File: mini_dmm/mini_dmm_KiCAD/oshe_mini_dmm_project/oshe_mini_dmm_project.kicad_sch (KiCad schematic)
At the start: 0 parts

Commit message: added to mini dmm schematic
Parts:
- added R1, R2, R3, R4: R_US, symbol Device:R_US
- added R5: 1, symbol Device:R_US
- added U1: LM358, symbol Amplifier_Operational:LM358
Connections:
- new net: R1.2, R2.1, U1.3 (+)
- new net: R3.1, R5.2
- new net: U1.1, U1.2 (-)
- new net: R3.2, R4.1, U1.5 (+)
- new net: U1.6 (-), U1.7
- new net GND: R2.2, R4.2

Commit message: Added to schematic
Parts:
- added BT1: Battery, symbol Device:Battery
- added F1: 500mA, symbol Device:Fuse_Small
- added F2: 1A, symbol Device:Fuse_Small
- added SW1: SW_DPDT_x2, symbol Switch:SW_DPDT_x2
- added U2: STM32F303CBTx, Package_QFP:LQFP-48_7x7mm_P0.5mm, symbol MCU_ST_STM32F3:STM32F303CBTx
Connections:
- net GND: now also BT1.2 (-)
- net at R1.1: now also F1.2
- net at R5.1: now also F2.2
- net Node_1: now reaches U1.1, U1.2 (-)
- net Node_2: now reaches U1.6 (-), U1.7
- net -3.3V: now reaches U1.4 (V-)
- net +3.3V: now reaches U1.8 (V+)
- net +3.3V: now also SW1.1 (A)
- new net: BT1.1 (+), SW1.2 (B)
- new net: U2.23 (VSS), U2.35 (VSS), U2.47 (VSS)
- no-connect marks 0 -> 1
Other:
- moved on the sheet: R1, R2, R3, R4, R5, U1A, U1B, U1C

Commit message: Made some more updates!
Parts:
- removed U1: LM358, symbol Amplifier_Operational:LM358
- added D1, D2, D3, D4: LED, symbol Device:LED
- added R6, R7, R8, R9: R_US, symbol Device:R_US
- added U1: LM324, Package_SO:SOIC-14_3.9x8.7mm_P1.27mm, symbol Amplifier_Operational:LM324
- renumbered R5 to R1, R1 to R2, R2 to R3, R3 to R4, R4 to R5
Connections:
- net +3.3V: now also U1.4 (V+)
- net -3.3V: now also U1.11 (V-)
- net GND: now also R7.2, R9.2
- net Node_1: now also U1.1, U1.2 (-)
- net Node_2: now also U1.6 (-), U1.7
- net at R2.2, R3.1: now also U1.3 (+)
- net at F2.2, R1.1: now also R6.1
- net at R1.2: now also R8.1; no longer R4.1
- net at R4.2, R5.1: now also U1.5 (+)
- new net: R8.2, R9.1, U1.12 (+)
- new net: R6.2, R7.1, U1.10 (+)
- new net Node_3: U1.8, U1.9 (-)
- new net Node_4: U1.13 (-), U1.14
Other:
- moved on the sheet: BT1, F2, R1, SW1A, U2

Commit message: made some updates
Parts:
- added R10, R11, R12, R13: 1k, symbol Device:R_US
- added SW2: MODE SELECT, symbol Switch:SW_Push
- D1: value LED -> VOLTAGE
- D2: value LED -> CURRENT
- D3: value LED -> RESISTANCE
- D4: value LED -> NEGATIVE
- R2, R4: value R_US -> 9.1MEG
- R3, R5, R7, R9: value R_US -> 1MEG
- R6, R8: value R_US -> 9MEG
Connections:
- net GND: now also R10.1, R11.1, R12.1, R13.1, SW2.2
- net at D4.1 (K): now also R13.2
- net at D4.2 (A): now also U2.13 (PA3)
- net at D2.1 (K): now also R11.2
- net at D2.2 (A): now also U2.11 (PA1)
- net at D3.1 (K): now also R12.2
- net at D3.2 (A): now also U2.12 (PA2)
- net at U2.10 (PA0): now also D1.2 (A)
- net at U2.14 (PA4): now also SW2.1
- net at D1.1 (K): now also R10.2
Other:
- moved on the sheet: BT1, D1, D2, D3, D4, SW1A, U2

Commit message: Updated schematic
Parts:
- added C1, C3, C4: 0.1uF, Capacitor_SMD:C_1206_3216Metric_Pad1.33x1.80mm_HandSolder, symbol Device:C
- added C5, C6: 22pF, Capacitor_SMD:C_1206_3216Metric_Pad1.33x1.80mm_HandSolder, symbol Device:C
- added D5: Green, LED_SMD:LED_1206_3216Metric_Pad1.42x1.75mm_HandSolder, symbol Device:LED
- added J1: FTDI Basic, Connector_PinSocket_2.54mm:PinSocket_1x06_P2.54mm_Vertical, symbol Connector_Generic:Conn_01x06
- added R14: 390, Resistor_SMD:R_1206_3216Metric_Pad1.30x1.75mm_HandSolder, symbol Device:R_US
- added R15: 10k, Resistor_SMD:R_1206_3216Metric_Pad1.30x1.75mm_HandSolder, symbol Device:R_US
- added SW3: PTS526 SK15 SMTR2 LFS, DMM_Footprint_Library:SMT_FS, symbol DMM_Symbol_Library:PTS526_SK15_SMTR2_LFS
- added U3: ATmega328P-A, Package_QFP:TQFP-32_7x7mm_P0.8mm, symbol MCU_Microchip_ATmega:ATmega328P-A
- added Y1: 16MHz, Crystal:Crystal_HC49-U_Vertical, symbol Device:Crystal
- R6, R8: value 9MEG -> 9.1MEG
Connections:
- net GND: now also C1.1, C3.2, C5.2, C6.1, D5.1 (K), J1.5 (Pin_5), J1.6 (Pin_6), SW3.3, SW3.4, U3.21 (GND), U3.3 (GND), U3.5 (GND)
- new net: C6.2, U3.8 (XTAL2/PB7), Y1.1
- new net: C4.1, R15.1, SW3.1, SW3.2, U3.29 (~{RESET}/PC6)
- new net: D5.2 (A), R14.1
- new net: C5.1, U3.7 (XTAL1/PB6), Y1.2
- new net: C1.2, U3.20 (AREF)
- new net +5V: C3.1, J1.4 (Pin_4), R15.2, U3.18 (AVCC), U3.4 (VCC), U3.6 (VCC)
- new net A0: U3.23 (PC0)
- new net A1: U3.24 (PC1)
- new net A2: U3.25 (PC2)
- new net A3: U3.26 (PC3)
- new net A6: U3.19 (ADC6)
- new net A7: U3.22 (ADC7)
- new net D10: U3.14 (PB2)
- new net D2: U3.32 (PD2)
- new net D3: U3.1 (PD3)
- new net D4: U3.2 (PD4)
- new net D5: U3.9 (PD5)
- new net D6: U3.10 (PD6)
- new net D7: U3.11 (PD7)
- new net D8: U3.12 (PB0)
- new net D9: U3.13 (PB1)
- new net DTR: C4.2, J1.1 (Pin_1)
- new net MISO/D12: U3.16 (PB4)
- new net MOSI/D11: U3.15 (PB3)
- new net RXD: J1.3 (Pin_3), U3.30 (PD0)
- new net SCK/D13: R14.2, U3.17 (PB5)
- new net SCL: U3.28 (PC5)
- new net SDA: U3.27 (PC4)
- new net TXD: J1.2 (Pin_2), U3.31 (PD1)
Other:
- note added: "ADD: - Convert arduino from 5V to 3.3V - Charge pump symbol and footprint - Display driver symbol (footprint already created) - resistance measurement stuff?"

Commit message: Made some more changes
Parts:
- removed SW3: PTS526 SK15 SMTR2 LFS, DMM_Footprint_Library:SMT_FS, symbol DMM_Symbol_Library:PTS526_SK15_SMTR2_LFS
- removed U2: STM32F303CBTx, Package_QFP:LQFP-48_7x7mm_P0.5mm, symbol MCU_ST_STM32F3:STM32F303CBTx
- added C2, C4, C5: 1uF, Capacitor_SMD:C_0805_2012Metric_Pad1.18x1.45mm_HandSolder, symbol Device:C
- added J2: DISPLAY, symbol Connector_Generic:Conn_01x12
- added R16: 300, Resistor_SMD:R_0805_2012Metric_Pad1.20x1.40mm_HandSolder, symbol Device:R_US
- added R17: 1k, Resistor_SMD:R_0805_2012Metric_Pad1.20x1.40mm_HandSolder, symbol Device:R_US
- added SW2: PTS526 SK15 SMTR2 LFS, DMM_Footprint_Library:SMT_FS, symbol Mini_DMM_Library:PTS526_SK15_SMTR2_LFS
- added U2: BU91796FS-ME2, Mini_DMM_Footprint_Library:SSOP-A32, symbol Mini_DMM_Library:BU91796FS-ME2
- added U4: LM2664M6, Mini_DMM_Footprint_Library:SOT95P280X145-6N, symbol Mini_DMM_Library:LM2664M6
- BT1: footprint (none) -> Battery:BatteryHolder_Keystone_3034_1x20mm
- C1, C3: footprint Capacitor_SMD:C_1206_3216Metric_Pad1.33x1.80mm_HandSolder -> Capacitor_SMD:C_0805_2012Metric_Pad1.18x1.45mm_HandSolder
- C6: renamed from C4; footprint Capacitor_SMD:C_1206_3216Metric_Pad1.33x1.80mm_HandSolder -> Capacitor_SMD:C_0805_2012Metric_Pad1.18x1.45mm_HandSolder
- C7: renamed from C5; footprint Capacitor_SMD:C_1206_3216Metric_Pad1.33x1.80mm_HandSolder -> Capacitor_SMD:C_0805_2012Metric_Pad1.18x1.45mm_HandSolder
- C8: renamed from C6; footprint Capacitor_SMD:C_1206_3216Metric_Pad1.33x1.80mm_HandSolder -> Capacitor_SMD:C_0805_2012Metric_Pad1.18x1.45mm_HandSolder
- D1, D2, D3, D4: footprint (none) -> LED_SMD:LED_0805_2012Metric_Pad1.15x1.40mm_HandSolder
- F1, F2: footprint (none) -> Fuse:Fuse_1206_3216Metric_Pad1.42x1.75mm_HandSolder
- R1: renamed from R2; footprint (none) -> Resistor_SMD:R_0805_2012Metric_Pad1.20x1.40mm_HandSolder
- R10, R11, R12, R13, R6, R7, R8, R9: footprint (none) -> Resistor_SMD:R_0805_2012Metric_Pad1.20x1.40mm_HandSolder
- R2: renamed from R3; footprint (none) -> Resistor_SMD:R_0805_2012Metric_Pad1.20x1.40mm_HandSolder
- R3: renamed from R4; footprint (none) -> Resistor_SMD:R_0805_2012Metric_Pad1.20x1.40mm_HandSolder
- R4: renamed from R5; footprint (none) -> Resistor_SMD:R_0805_2012Metric_Pad1.20x1.40mm_HandSolder
- R5: renamed from R1; footprint (none) -> Resistor_SMD:R_2512_6332Metric_Pad1.40x3.35mm_HandSolder
- renumbered SW2 to SW1, SW1 to SW3
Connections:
- net +5V is gone; now on net +3.3V: C3.1, J1.4 (Pin_4), R15.2, U3.18 (AVCC), U3.4 (VCC), U3.6 (VCC)
- net Node_1 is gone; now on net A0: U1.1, U1.2 (-)
- net Node_2 is gone; now on net A1: U1.6 (-), U1.7
- net Node_3 is gone; now on net A2: U1.8, U1.9 (-)
- net Node_4 is gone; now on net A3: U1.13 (-), U1.14
- net +3.3V: now also C4.2, R16.1, U2.24 (VDD), U4.4 (~{SD}), U4.5 (V+)
- net -3.3V: now also C5.2, U4.2 (OUT)
- net D2: now also D1.2 (A)
- net D3: now also D2.2 (A)
- net D4: now also D3.2 (A)
- net D5: now also D4.2 (A)
- net D6: now also SW1.1
- net GND: now also C4.1, C5.1, R17.2, SW2.3, SW2.4, U2.25 (VSS), U4.1 (GND)
- net LEAD_4: now reaches R5.2, R8.1
- net at C6.1, R15.1, U3.29 (~{RESET}/PC6): now also SW2.1, SW2.2
- net LEAD_1: now reaches F1.1
- net LEAD_3: now reaches F2.1
- net LEAD_2: now reaches R3.1
- net SCL renamed A5/SCL
- net SDA renamed A4/SDA
- new net: R16.2, R17.1, U2.23 (VLCD)
- new net: C2.1, U4.6 (CAP+)
- new net: C2.2, U4.3 (CAP-)
- new net COM0: J2.1 (Pin_1), U2.19 (COM_0)
- new net COM1: J2.2 (Pin_2), U2.20 (COM_1)
- new net COM2: J2.3 (Pin_3), U2.21 (COM_2)
- new net COM3: J2.4 (Pin_4), U2.22 (COM_3)
- new net SEG0: J2.5 (Pin_5), U2.31 (SEG_0)
- new net SEG1: J2.6 (Pin_6), U2.32 (SEG_1)
- new net SEG2: J2.7 (Pin_7), U2.1 (SEG_2)
- new net SEG3: J2.8 (Pin_8), U2.2 (SEG_3)
- new net SEG4: J2.9 (Pin_9), U2.3 (SEG_4)
- new net SEG5: J2.10 (Pin_10), U2.4 (SEG_5)
- new net SEG6: J2.11 (Pin_11), U2.5 (SEG_6)
- new net SEG7: J2.12 (Pin_12), U2.6 (SEG_7)
- no-connect marks 1 -> 16
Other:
- note added: "NOTE: potentially experiment with summing both current and voltage into the same analog pins?"
- note added: "VLCD wants 2.45 V or higher Voltage Divider to create 2.53 V"
- note removed: "ADD: - Convert arduino from 5V to 3.3V - Charge pump symbol and footprint - Display driver symbol (footprint already created) - resistance measurement stuff?"
- moved on the sheet: BT1, C1, C3, C6, C7, C8, D1, D2, D3, D4, D5, F1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

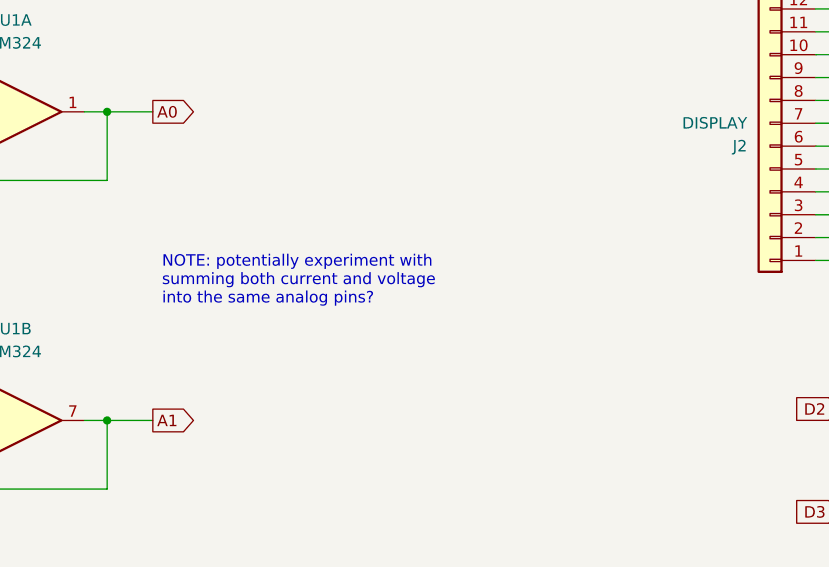
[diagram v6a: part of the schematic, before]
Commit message: Exported a BoM
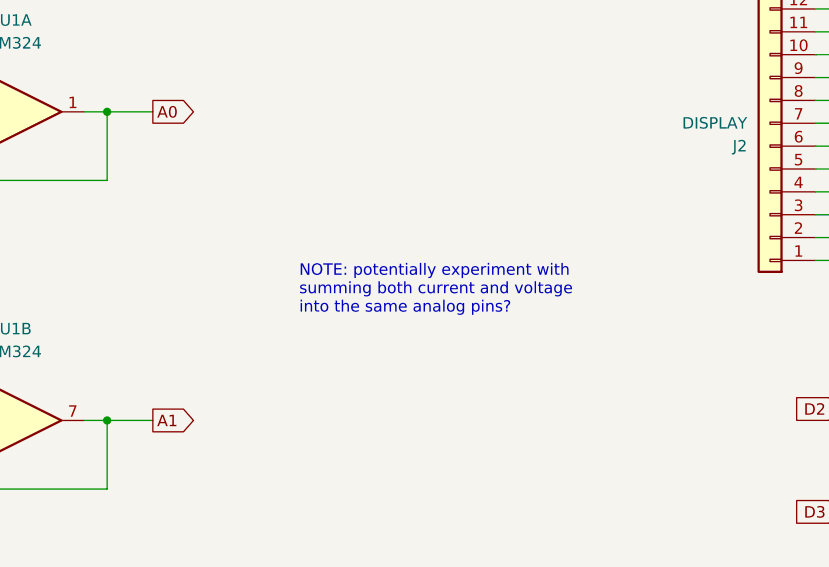
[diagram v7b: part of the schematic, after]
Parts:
- D5: footprint LED_SMD:LED_1206_3216Metric_Pad1.42x1.75mm_HandSolder -> LED_SMD:LED_0805_2012Metric_Pad1.15x1.40mm_HandSolder
- R14, R15: footprint Resistor_SMD:R_1206_3216Metric_Pad1.30x1.75mm_HandSolder -> Resistor_SMD:R_0805_2012Metric_Pad1.20x1.40mm_HandSolder
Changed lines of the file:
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@@
 	(text "NOTE: potentially experiment with \nsumming both current and voltage \ninto the same analog pins?"
 		(exclude_from_sim no)
-		(at 93.726 65.786 0)
+		(at 108.966 66.802 0)
 		(effects
 			(font
@@
 			)
 		)
-		(property "Footprint" "Resistor_SMD:R_1206_3216Metric_Pad1.30x1.75mm_HandSolder"
+		(property "Footprint" "Resistor_SMD:R_0805_2012Metric_Pad1.20x1.40mm_HandSolder"
 			(at 399.796 193.294 90)
 			(effects
@@
 			)
 		)
-		(property "Footprint" "Resistor_SMD:R_1206_3216Metric_Pad1.30x1.75mm_HandSolder"
+		(property "Footprint" "Resistor_SMD:R_0805_2012Metric_Pad1.20x1.40mm_HandSolder"
 			(at 385.826 145.034 90)
 			(effects
@@
 			)
 		)
-		(property "Footprint" "LED_SMD:LED_1206_3216Metric_Pad1.42x1.75mm_HandSolder"
+		(property "Footprint" "LED_SMD:LED_0805_2012Metric_Pad1.15x1.40mm_HandSolder"
 			(at 396.24 146.05 0)
 			(effects

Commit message: Updated Schematic
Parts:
- removed R6, R8: 9.1MEG, Resistor_SMD:R_0805_2012Metric_Pad1.20x1.40mm_HandSolder, symbol Device:R_US
- removed R7, R9: 1MEG, Resistor_SMD:R_0805_2012Metric_Pad1.20x1.40mm_HandSolder, symbol Device:R_US
- added F3: 500mA, Fuse:Fuse_1206_3216Metric_Pad1.42x1.75mm_HandSolder, symbol Device:Fuse_Small
- added J3: TEST LEAD CONNECTIONS, symbol Connector_Generic:Conn_01x06
- R5: value 1 -> 0.05
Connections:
- net LEAD_1: now also J3.1 (Pin_1)
- net LEAD_2: now also F3.1, J3.2 (Pin_2); no longer R3.1
- net LEAD_3: now also J3.3 (Pin_3)
- net LEAD_4: now also U1.12 (+), J3.4 (Pin_4)
- net at F2.2, R5.1: now also U1.10 (+)
- new net: F3.2, R3.1
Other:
- note added: "Add in pins to flash IC"
- note added: "NOTE: potentially experiment with summing both current and voltage into the same analog pins? BEN's NOTE: Looking at Op amp current draw?"
- note added: "Resistance?"
- note added: "USB Support?"
- note removed: "NOTE: potentially experiment with summing both current and voltage into the same analog pins?"
- moved on the sheet: U1C, U1D, U1E
